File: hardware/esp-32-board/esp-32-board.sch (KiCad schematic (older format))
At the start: 13 parts, among them J1 ESP-PROG-Program, J2 MainConnector, J3 ESP-PROG-Debug, J4 Conn_01x06, SW1 SW_Push, SW2 SW_Push, U1 ESP32-WROOM-32

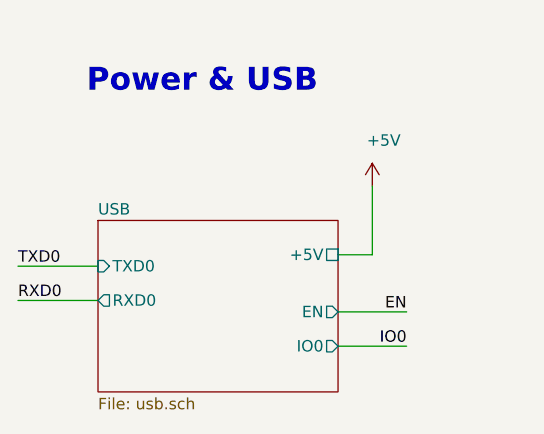
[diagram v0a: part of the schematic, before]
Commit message: Swap RX and TX on FT232RL
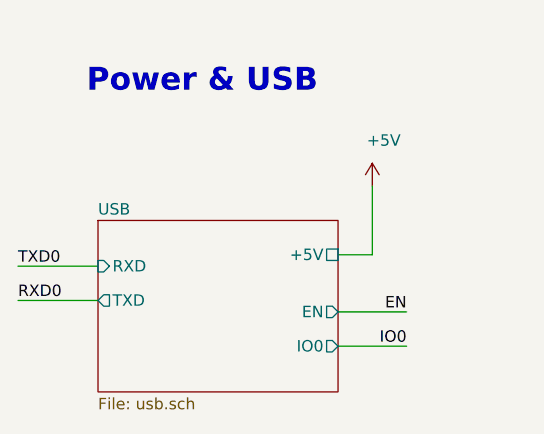
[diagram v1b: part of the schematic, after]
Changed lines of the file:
@@
 F2 "EN" O R 2300 6650 50
 F3 "IO0" O R 2300 6800 50
-F4 "TXD0" I L 1250 6450 50
-F5 "RXD0" O L 1250 6600 50
-F6 "+5V" U R 2300 6400 50
+F4 "+5V" U R 2300 6400 50
+F5 "RXD" I L 1250 6450 50
+F6 "TXD" O L 1250 6600 50
 $EndSheet
 Text Label 2600 6800 2    50   ~ 0

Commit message: Use 1206 resistor array for RN1
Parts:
- RN1: footprint Resistor_SMD:R_Array_Convex_4x1206 -> Resistor_SMD:R_Array_Convex_4x0612
- RN1: footprint Resistor_SMD:R_Array_Convex_4x1206 -> Resistor_SMD:R_Array_Convex_4x0612; VendorLink https://www.tme.eu/pl/en/details/dr0804-100r-4_8/smd-resist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 -> https://www.tme.eu/pl/details/dr1206-100r-4_8/drabinki-rezy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
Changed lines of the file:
@@
 F 0 "RN1" V 9900 5350 50  0000 C CNN
 F 1 "100 Ohm" V 9900 5900 50  0000 C CNN
-F 2 "Resistor_SMD:R_Array_Convex_4x1206" V 9870 5600 50  0001 C CNN
-F 3 "~" H 9950 5600 50  0001 C CNN
+F 2 "Resistor_SMD:R_Array_Convex_4x0612" V 9870 5600 50  0001 C CNN
+F 3 "https://www.tme.eu/Document/06db5b489d2b0c3473dd3a4d90f1faf2/ROYALOHM-xDx.pdf" H 9950 5600 50  0001 C CNN
 F 4 "tme.eu" H 9950 5600 50  0001 C CNN "Vendor"
 F 5 "https://www.tme.eu/pl/en/details/dr0804-100r-4_8/smd-resistor-networks/royal-ohm/4d02wgj0101t/" H 9950 5600 50  0001 C CNN "VendorLink"
@@
 F 0 "RN1" V 9900 5250 50  0000 C CNN
 F 1 "100 Ohm" V 9900 5800 50  0000 C CNN
-F 2 "Resistor_SMD:R_Array_Convex_4x1206" V 9870 5500 50  0001 C CNN
-F 3 "~" H 9950 5500 50  0001 C CNN
+F 2 "Resistor_SMD:R_Array_Convex_4x0612" V 9870 5500 50  0001 C CNN
+F 3 "https://www.tme.eu/Document/06db5b489d2b0c3473dd3a4d90f1faf2/ROYALOHM-xDx.pdf" H 9950 5500 50  0001 C CNN
 F 4 "tme.eu" H 9950 5500 50  0001 C CNN "Vendor"
 F 5 "https://www.tme.eu/pl/en/details/dr0804-100r-4_8/smd-resistor-networks/royal-ohm/4d02wgj0101t/" H 9950 5500 50  0001 C CNN "VendorLink"
@@
 F 0 "RN1" V 9900 5150 50  0000 C CNN
 F 1 "100 Ohm" V 9900 5700 50  0000 C CNN
-F 2 "Resistor_SMD:R_Array_Convex_4x1206" V 9870 5400 50  0001 C CNN
-F 3 "~" H 9950 5400 50  0001 C CNN
+F 2 "Resistor_SMD:R_Array_Convex_4x0612" V 9870 5400 50  0001 C CNN
+F 3 "https://www.tme.eu/Document/06db5b489d2b0c3473dd3a4d90f1faf2/ROYALOHM-xDx.pdf" H 9950 5400 50  0001 C CNN
 F 4 "tme.eu" H 9950 5400 50  0001 C CNN "Vendor"
-F 5 "https://www.tme.eu/pl/en/details/dr0804-100r-4_8/smd-resistor-networks/royal-ohm/4d02wgj0101t/" H 9950 5400 50  0001 C CNN "VendorLink"
+F 5 "https://www.tme.eu/pl/details/dr1206-100r-4_8/drabinki-rezystorowe-smd/royal-ohm/4d03wgj0101t5e/" H 9950 5400 50  0001 C CNN "VendorLink"
 	3    9950 5400
 	0    1    1    0
@@
 F 0 "RN1" V 9900 5450 50  0000 C CNN
 F 1 "100 Ohm" V 9900 6000 50  0000 C CNN
-F 2 "Resistor_SMD:R_Array_Convex_4x1206" V 9870 5700 50  0001 C CNN
-F 3 "~" H 9950 5700 50  0001 C CNN
+F 2 "Resistor_SMD:R_Array_Convex_4x0612" V 9870 5700 50  0001 C CNN
+F 3 "https://www.tme.eu/Document/06db5b489d2b0c3473dd3a4d90f1faf2/ROYALOHM-xDx.pdf" H 9950 5700 50  0001 C CNN
 F 4 "tme.eu" H 9950 5700 50  0001 C CNN "Vendor"
 F 5 "https://www.tme.eu/pl/en/details/dr0804-100r-4_8/smd-resistor-networks/royal-ohm/4d02wgj0101t/" H 9950 5700 50  0001 C CNN "VendorLink"

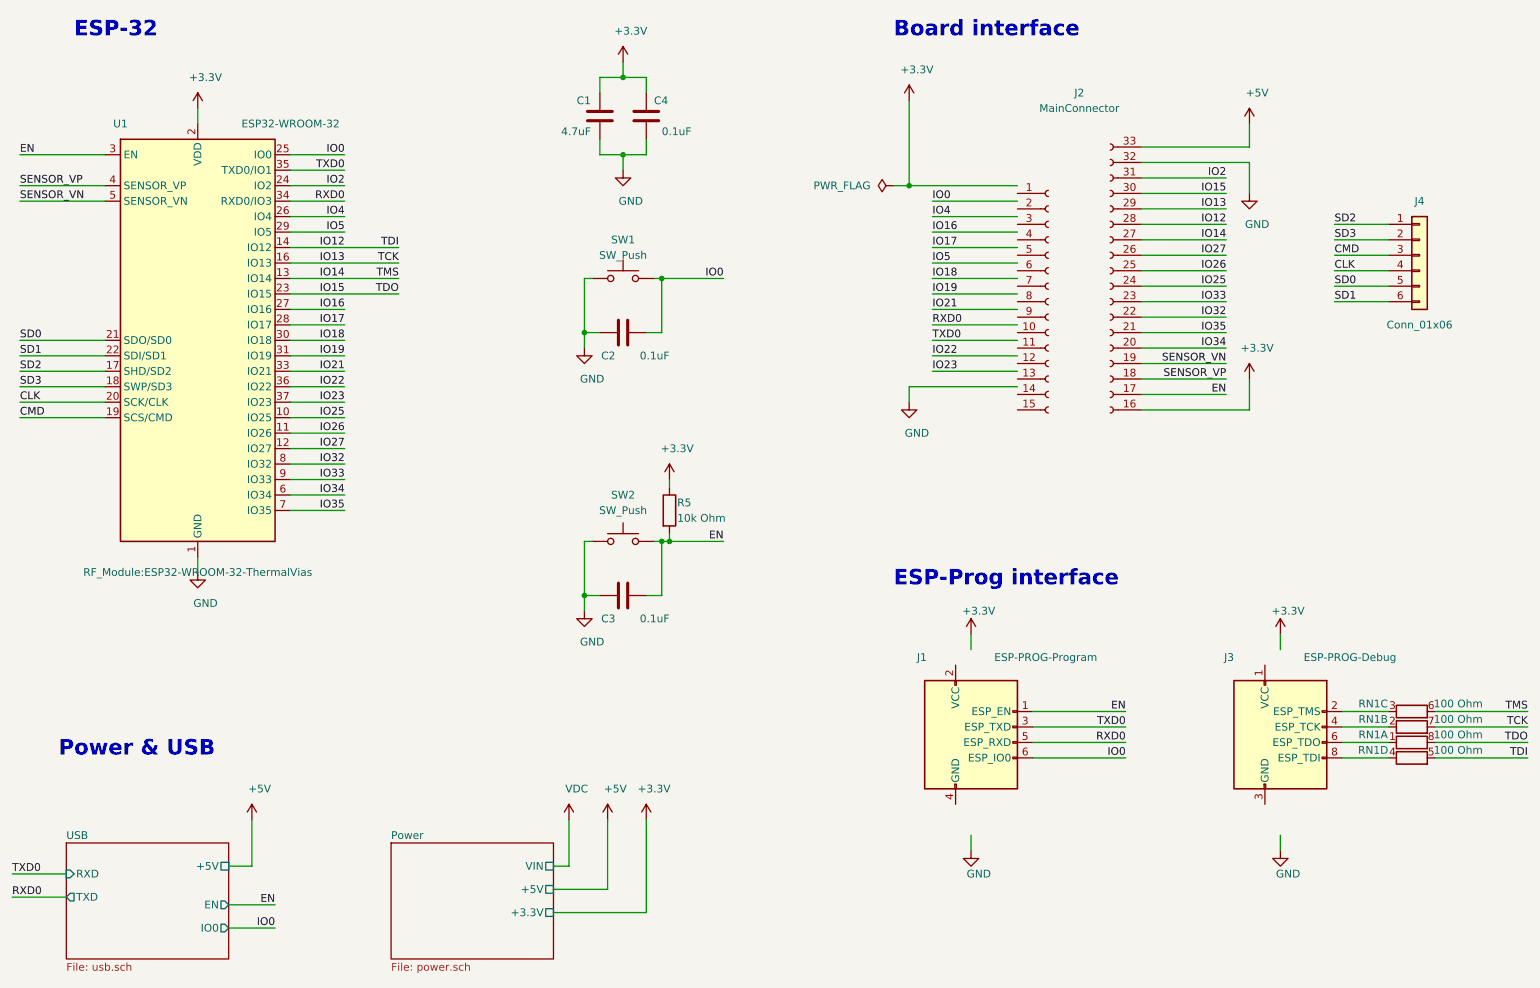
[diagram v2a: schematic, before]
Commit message: Move ESP-PROG ports
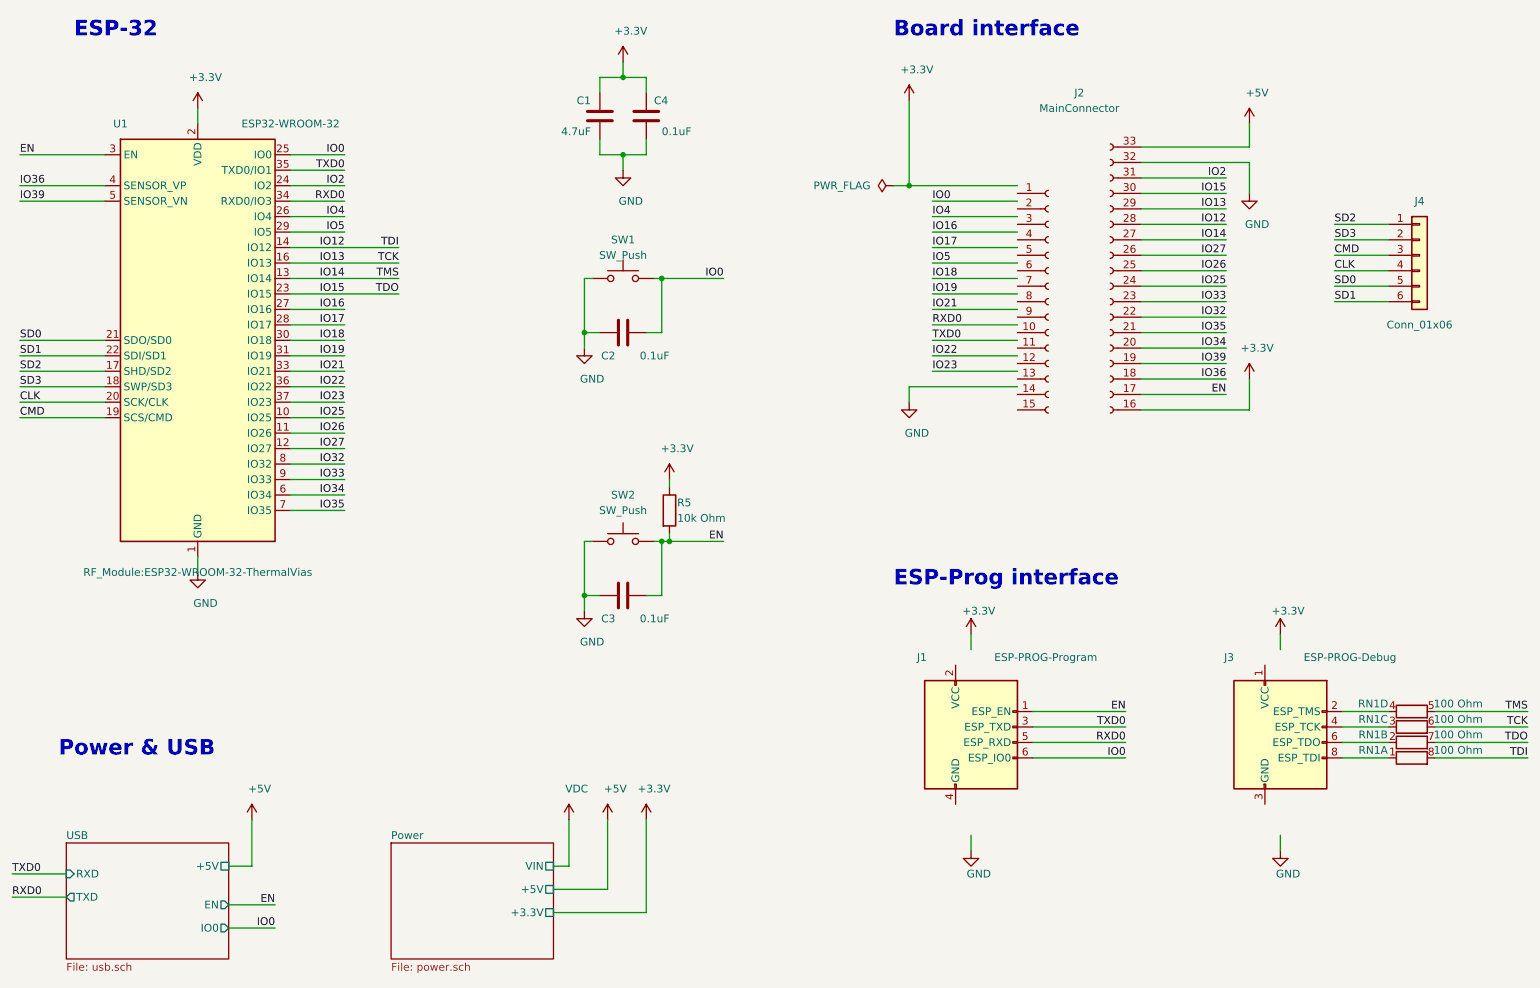
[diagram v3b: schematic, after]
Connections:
- net labels added: IO36, IO39
- net labels removed: SENSOR_VN, SENSOR_VP
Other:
- moved on the sheet: RN1A, RN1B, RN1C, RN1D
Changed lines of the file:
@@
 EN
 Text Label 8750 3250 2    50   ~ 0
-SENSOR_VP
+IO36
 Text Label 8750 3150 2    50   ~ 0
-SENSOR_VN
+IO39
 Text Label 8750 3050 2    50   ~ 0
 IO34
@@
 EN
 Text Label 950  2000 0    50   ~ 0
-SENSOR_VP
+IO36
 Text Label 950  2100 0    50   ~ 0
-SENSOR_VN
+IO39
 Text Label 950  3000 0    50   ~ 0
 SD0
@@
 L Device:R_Pack04_Split RN1
 U 1 1 6008D4E8
+P 9950 5700
+F 0 "RN1" V 9900 5450 50  0000 C CNN
+F 1 "100 Ohm" V 9900 6000 50  0000 C CNN
+F 2 "Resistor_SMD:R_Array_Convex_4x0612" V 9870 5700 50  0001 C CNN
+F 3 "https://www.tme.eu/Document/06db5b489d2b0c3473dd3a4d90f1faf2/ROYALOHM-xDx.pdf" H 9950 5700 50  0001 C CNN
+F 4 "tme.eu" H 9950 5700 50  0001 C CNN "Vendor"
+F 5 "https://www.tme.eu/pl/en/details/dr0804-100r-4_8/smd-resistor-networks/royal-ohm/4d02wgj0101t/" H 9950 5700 50  0001 C CNN "VendorLink"
+	1    9950 5700
+	0    1    1    0
+$EndComp
+$Comp
+L Device:R_Pack04_Split RN1
+U 2 1 6008EB1A
 P 9950 5600
 F 0 "RN1" V 9900 5350 50  0000 C CNN
@@
 F 4 "tme.eu" H 9950 5600 50  0001 C CNN "Vendor"
 F 5 "https://www.tme.eu/pl/en/details/dr0804-100r-4_8/smd-resistor-networks/royal-ohm/4d02wgj0101t/" H 9950 5600 50  0001 C CNN "VendorLink"
-	1    9950 5600
+	2    9950 5600
 	0    1    1    0
 $EndComp
 $Comp
 L Device:R_Pack04_Split RN1
-U 2 1 6008EB1A
+U 3 1 6008F771
 P 9950 5500
 F 0 "RN1" V 9900 5250 50  0000 C CNN
@@
 F 3 "https://www.tme.eu/Document/06db5b489d2b0c3473dd3a4d90f1faf2/ROYALOHM-xDx.pdf" H 9950 5500 50  0001 C CNN
 F 4 "tme.eu" H 9950 5500 50  0001 C CNN "Vendor"
-F 5 "https://www.tme.eu/pl/en/details/dr0804-100r-4_8/smd-resistor-networks/royal-ohm/4d02wgj0101t/" H 9950 5500 50  0001 C CNN "VendorLink"
-	2    9950 5500
+F 5 "https://www.tme.eu/pl/details/dr1206-100r-4_8/drabinki-rezystorowe-smd/royal-ohm/4d03wgj0101t5e/" H 9950 5500 50  0001 C CNN "VendorLink"
+	3    9950 5500
 	0    1    1    0
 $EndComp
 $Comp
 L Device:R_Pack04_Split RN1
-U 3 1 6008F771
+U 4 1 600907AD
 P 9950 5400
 F 0 "RN1" V 9900 5150 50  0000 C CNN
@@
 F 3 "https://www.tme.eu/Document/06db5b489d2b0c3473dd3a4d90f1faf2/ROYALOHM-xDx.pdf" H 9950 5400 50  0001 C CNN
 F 4 "tme.eu" H 9950 5400 50  0001 C CNN "Vendor"
-F 5 "https://www.tme.eu/pl/details/dr1206-100r-4_8/drabinki-rezystorowe-smd/royal-ohm/4d03wgj0101t5e/" H 9950 5400 50  0001 C CNN "VendorLink"
-	3    9950 5400
+F 5 "https://www.tme.eu/pl/en/details/dr0804-100r-4_8/smd-resistor-networks/royal-ohm/4d02wgj0101t/" H 9950 5400 50  0001 C CNN "VendorLink"
+	4    9950 5400
 	0    1    1    0
 $EndComp
-$Comp
-L Device:R_Pack04_Split RN1
-U 4 1 600907AD
-P 9950 5700
-F 0 "RN1" V 9900 5450 50  0000 C CNN
-F 1 "100 Ohm" V 9900 6000 50  0000 C CNN
-F 2 "Resistor_SMD:R_Array_Convex_4x0612" V 9870 5700 50  0001 C CNN
-F 3 "https://www.tme.eu/Document/06db5b489d2b0c3473dd3a4d90f1faf2/ROYALOHM-xDx.pdf" H 9950 5700 50  0001 C CNN
-F 4 "tme.eu" H 9950 5700 50  0001 C CNN "Vendor"
-F 5 "https://www.tme.eu/pl/en/details/dr0804-100r-4_8/smd-resistor-networks/royal-ohm/4d02wgj0101t/" H 9950 5700 50  0001 C CNN "VendorLink"
-	4    9950 5700
-	0    1    1    0
-$EndComp

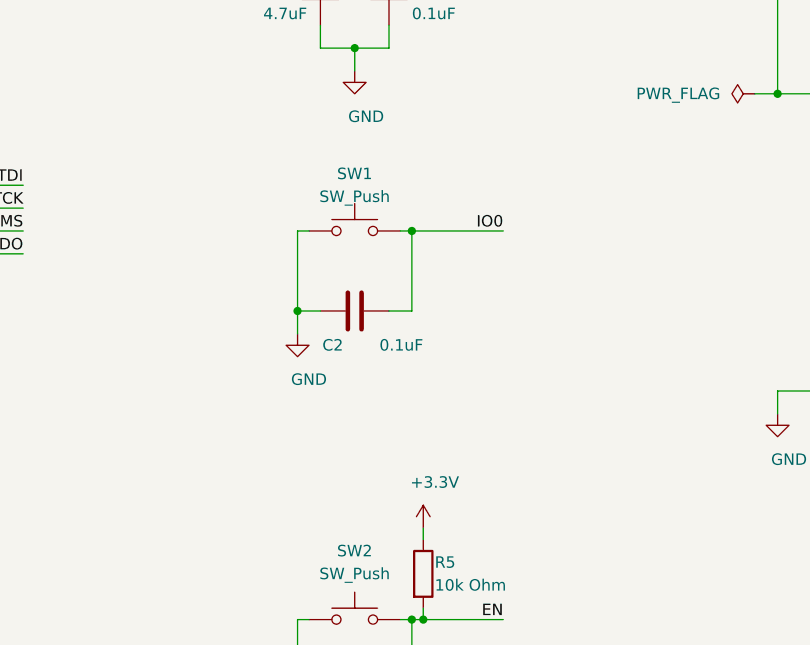
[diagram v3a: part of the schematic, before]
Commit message: Add pullup for IO0
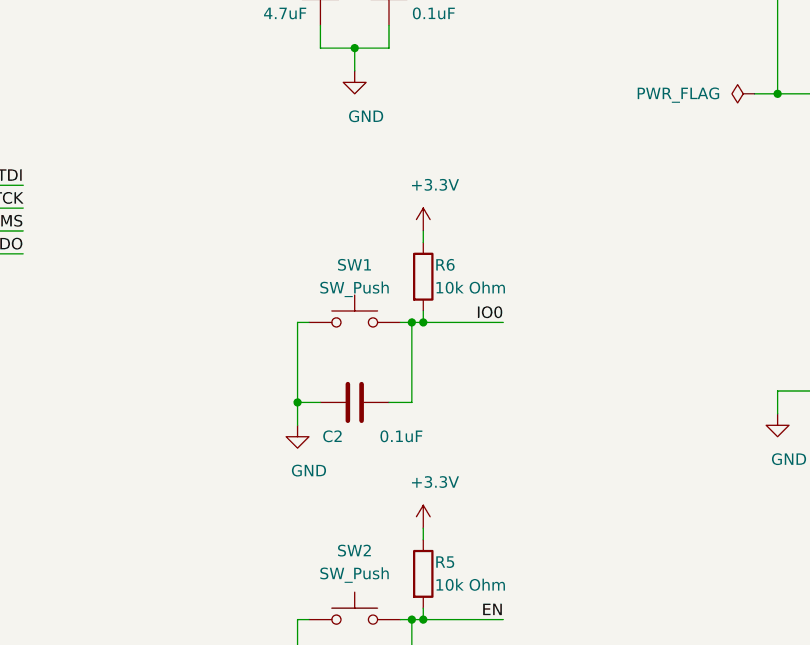
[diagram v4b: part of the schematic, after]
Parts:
- added R6: 10k Ohm, Resistor_SMD:R_0805_2012Metric_Pad1.20x1.40mm_HandSolder, symbol Device:R
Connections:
- wire segments 136 -> 139
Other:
- moved on the sheet: C2, SW1
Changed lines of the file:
@@
 L Device:C C2
 U 1 1 5FAC9D96
-P 4850 2950
-F 0 "C2" V 4700 3000 50  0000 L CNN
-F 1 "0.1uF" V 4700 2650 50  0000 L CNN
-F 2 "Capacitor_SMD:C_0805_2012Metric_Pad1.18x1.45mm_HandSolder" H 4888 2800 50  0001 C CNN
-F 3 "~" H 4850 2950 50  0001 C CNN
-F 4 "avt.pl" H 4850 2950 50  0001 C CNN "Vendor"
-F 5 "https://sklep.avt.pl/zestaw-kondensatorow-smd-0805-720-sztuk.html" H 4850 2950 50  0001 C CNN "VendorLink"
-	1    4850 2950
+P 4850 3350
+F 0 "C2" V 4700 3400 50  0000 L CNN
+F 1 "0.1uF" V 4700 3050 50  0000 L CNN
+F 2 "Capacitor_SMD:C_0805_2012Metric_Pad1.18x1.45mm_HandSolder" H 4888 3200 50  0001 C CNN
+F 3 "~" H 4850 3350 50  0001 C CNN
+F 4 "avt.pl" H 4850 3350 50  0001 C CNN "Vendor"
+F 5 "https://sklep.avt.pl/zestaw-kondensatorow-smd-0805-720-sztuk.html" H 4850 3350 50  0001 C CNN "VendorLink"
+	1    4850 3350
 	0    -1   -1   0
 $EndComp
@@
 L Switch:SW_Push SW1
 U 1 1 5FB57488
-P 4850 2600
-F 0 "SW1" H 4850 2850 50  0000 C CNN
-F 1 "SW_Push" H 4850 2750 50  0000 C CNN
-F 2 "Button_Switch_SMD:SW_Push_1P1T_NO_6x6mm_H4.3mm" H 4850 2800 50  0001 C CNN
-F 3 "" H 4850 2800 50  0001 C CNN
-F 4 "tme.eu" H 4850 2600 50  0001 C CNN "Vendor"
-F 5 "https://www.tme.eu/pl/details/b3s-1000/mikroprzelaczniki-tact/omron-ocb/" H 4850 2600 50  0001 C CNN "VendorLink"
-	1    4850 2600
+P 4850 3000
+F 0 "SW1" H 4850 3250 50  0000 C CNN
+F 1 "SW_Push" H 4850 3150 50  0000 C CNN
+F 2 "Button_Switch_SMD:SW_Push_1P1T_NO_6x6mm_H4.3mm" H 4850 3200 50  0001 C CNN
+F 3 "" H 4850 3200 50  0001 C CNN
+F 4 "tme.eu" H 4850 3000 50  0001 C CNN "Vendor"
+F 5 "https://www.tme.eu/pl/details/b3s-1000/mikroprzelaczniki-tact/omron-ocb/" H 4850 3000 50  0001 C CNN "VendorLink"
+	1    4850 3000
 	1    0    0    -1
 $EndComp
@@
 Connection ~ 5100 4300
 Wire Wire Line
-	4650 2600 4600 2600
-Wire Wire Line
-	4600 2600 4600 2950
-Wire Wire Line
-	4700 2950 4600 2950
-Connection ~ 4600 2950
-Wire Wire Line
-	4600 2950 4600 3050
-Wire Wire Line
-	5050 2600 5100 2600
-Wire Wire Line
-	5100 2600 5100 2950
-Wire Wire Line
-	5100 2950 5000 2950
-Wire Wire Line
-	5100 2600 5500 2600
-Connection ~ 5100 2600
+	4650 3000 4600 3000
+Wire Wire Line
+	4600 3000 4600 3350
+Wire Wire Line
+	4700 3350 4600 3350
+Connection ~ 4600 3350
+Wire Wire Line
+	4600 3350 4600 3450
+Wire Wire Line
+	5050 3000 5100 3000
+Wire Wire Line
+	5100 3000 5100 3350
+Wire Wire Line
+	5100 3350 5000 3350
+Wire Wire Line
+	5100 3000 5150 3000
+Connection ~ 5100 3000
 $Comp
 L power:GND #PWR05
 U 1 1 5FB79B18
-P 4600 3050
-F 0 "#PWR05" H 4600 2800 50  0001 C CNN
-F 1 "GND" H 4650 2850 50  0000 C CNN
-F 2 "" H 4600 3050 50  0001 C CNN
-F 3 "" H 4600 3050 50  0001 C CNN
-	1    4600 3050
+P 4600 3450
+F 0 "#PWR05" H 4600 3200 50  0001 C CNN
+F 1 "GND" H 4650 3250 50  0000 C CNN
+F 2 "" H 4600 3450 50  0001 C CNN
+F 3 "" H 4600 3450 50  0001 C CNN
+	1    4600 3450
 	1    0    0    -1
 $EndComp
@@
 	1    0    0    -1
 $EndComp
-Text Label 5500 2600 2    50   ~ 0
+Text Label 5500 3000 2    50   ~ 0
 IO0
 Text Label 5500 4300 2    50   ~ 0
@@
 	1    0    0    -1
 $EndComp
+Wire Wire Line
+	5150 2600 5150 2650
+$Comp
+L Device:R R6
+U 1 1 604EEDDB
+P 5150 2800
+F 0 "R6" H 5200 2850 50  0000 L CNN
+F 1 "10k Ohm" H 5200 2750 50  0000 L CNN
+F 2 "Resistor_SMD:R_0805_2012Metric_Pad1.20x1.40mm_HandSolder" V 5080 2800 50  0001 C CNN
+F 3 "~" H 5150 2800 50  0001 C CNN
+F 4 "avt.pl" H 5150 2800 50  0001 C CNN "Vendor"
+F 5 "https://sklep.avt.pl/avt701-805.html" H 5150 2800 50  0001 C CNN "VendorLink"
+	1    5150 2800
+	1    0    0    -1
+$EndComp
+$Comp
+L power:+3.3V #PWR027
+U 1 1 604EEDE1
+P 5150 2600
+F 0 "#PWR027" H 5150 2450 50  0001 C CNN
+F 1 "+3.3V" H 5200 2800 50  0000 C CNN
+F 2 "" H 5150 2600 50  0001 C CNN
+F 3 "" H 5150 2600 50  0001 C CNN
+	1    5150 2600
+	1    0    0    -1
+$EndComp
+Wire Wire Line
+	5150 2950 5150 3000
+Connection ~ 5150 3000
+Wire Wire Line
+	5150 3000 5500 3000
 $EndSCHEMATC

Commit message: Fix ERC error
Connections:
- wire segments 139 -> 138
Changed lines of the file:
@@
 Wire Wire Line
 	5000 6100 5000 6700
-$Comp
-L power:PWR_FLAG #FLG01
-U 1 1 5FD0B643
-P 6600 2000
-F 0 "#FLG01" H 6600 2075 50  0001 C CNN
-F 1 "PWR_FLAG" V 6600 2150 50  0000 L CNN
-F 2 "" H 6600 2000 50  0001 C CNN
-F 3 "~" H 6600 2000 50  0001 C CNN
-	1    6600 2000
-	0    -1   -1   0
-$EndComp
-Wire Wire Line
-	6600 2000 6700 2000
-Connection ~ 6700 2000
 Wire Wire Line
 	2100 4400 2100 4500

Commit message: CI: fix errors (#2)
* CI: fix errors

* Cosmetic fixes on PCB

* Change build trigger conditions

* Regenerate cooper zones

* Cosmetic fixes on PCB

* Mark ESP-PROG as SMD
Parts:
- R5, R6: value 10k Ohm -> 10 kOhm
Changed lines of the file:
@@
 P 5150 4100
 F 0 "R5" H 5200 4150 50  0000 L CNN
-F 1 "10k Ohm" H 5200 4050 50  0000 L CNN
+F 1 "10 kOhm" H 5200 4050 50  0000 L CNN
 F 2 "Resistor_SMD:R_0805_2012Metric_Pad1.20x1.40mm_HandSolder" V 5080 4100 50  0001 C CNN
 F 3 "~" H 5150 4100 50  0001 C CNN
@@
 P 5150 2800
 F 0 "R6" H 5200 2850 50  0000 L CNN
-F 1 "10k Ohm" H 5200 2750 50  0000 L CNN
+F 1 "10 kOhm" H 5200 2750 50  0000 L CNN
 F 2 "Resistor_SMD:R_0805_2012Metric_Pad1.20x1.40mm_HandSolder" V 5080 2800 50  0001 C CNN
 F 3 "~" H 5150 2800 50  0001 C CNN
